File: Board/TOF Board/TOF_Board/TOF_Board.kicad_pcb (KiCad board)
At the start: 2 copper layers, 9 parts, among them J1 140-506-415-000, U1 VL53L1CBV0FY-1, U2 AT30TS74-XM8M-T

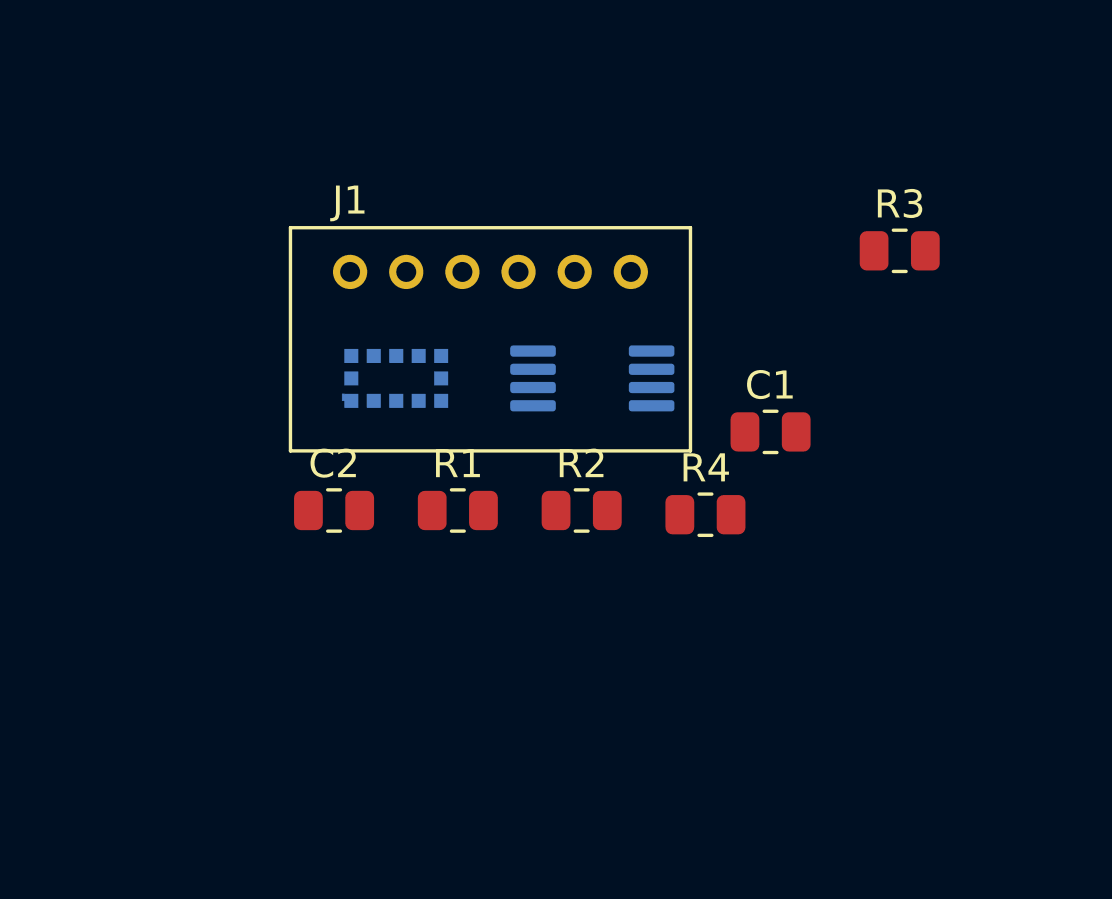
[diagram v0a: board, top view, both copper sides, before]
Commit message: added top load connector
Signed-off-by: EricTheGreat <joesmith01110000011101010111@gmail.com>
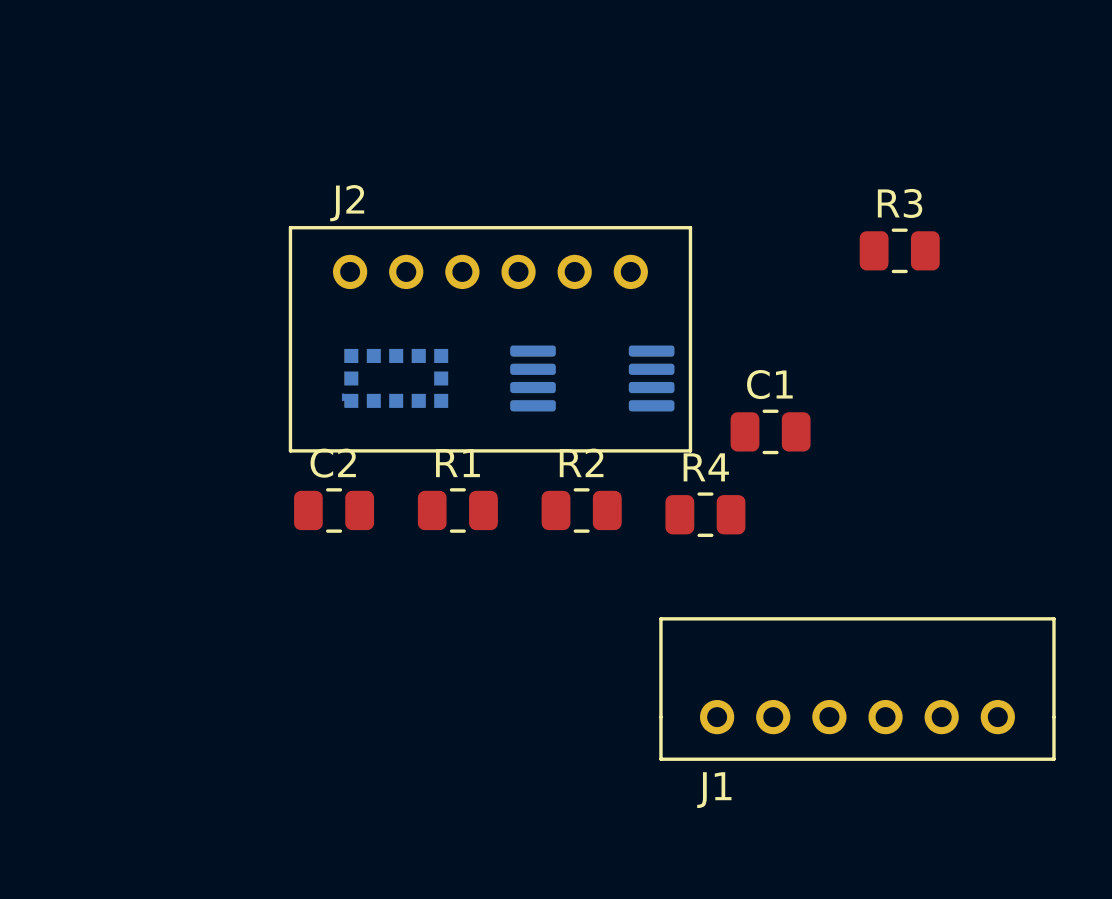
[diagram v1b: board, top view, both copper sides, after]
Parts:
- added J1: 140-506-415-001, KiCad_Cust:140-506-415-001, F.Cu at (89.5, 67.9)
- renumbered J1 to J2
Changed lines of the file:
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@@
   (net 20 "unconnected-(U2-Pad7)")
   (net 21 "unconnected-(U2-Pad8)")
+  (net 22 "unconnected-(J2-Pad1)")
+  (net 23 "unconnected-(J2-Pad2)")
+  (net 24 "unconnected-(J2-Pad3)")
+  (net 25 "unconnected-(J2-Pad4)")
+  (net 26 "unconnected-(J2-Pad5)")
+  (net 27 "unconnected-(J2-Pad6)")
   (footprint "Resistor_SMD:R_0805_2012Metric" (layer "F.Cu")
     (at 89.12 60.735)
@@
     (property "Sheetname" "")
     (attr through_hole)
-    (fp_text reference "J1" (at 0 -2.54) (layer "F.SilkS")
+    (fp_text reference "J2" (at 0 -2.54) (layer "F.SilkS")
       (effects (font (size 1 1) (thickness 0.15)))
     )
@@
     (fp_line (start -1.9977 6.2484) (end 11.9977 6.2484) (layer "F.Fab") (width 0.1))
     (pad "1" thru_hole circle (at 0 0) (size 1.2192 1.2192) (drill 0.7112) (layers *.Cu *.Mask)
+      (net 22 "unconnected-(J2-Pad1)") (pinfunction "1") (pintype "unspecified"))
+    (pad "2" thru_hole circle (at 2.000001 0) (size 1.2192 1.2192) (drill 0.7112) (layers *.Cu *.Mask)
+      (net 23 "unconnected-(J2-Pad2)") (pinfunction "2") (pintype "unspecified"))
+    (pad "3" thru_hole circle (at 4 0) (size 1.2192 1.2192) (drill 0.7112) (layers *.Cu *.Mask)
+      (net 24 "unconnected-(J2-Pad3)") (pinfunction "3") (pintype "unspecified"))
+    (pad "4" thru_hole circle (at 6.000001 0) (size 1.2192 1.2192) (drill 0.7112) (layers *.Cu *.Mask)
+      (net 25 "unconnected-(J2-Pad4)") (pinfunction "4") (pintype "unspecified"))
+    (pad "5" thru_hole circle (at 7.999999 0) (size 1.2192 1.2192) (drill 0.7112) (layers *.Cu *.Mask)
+      (net 26 "unconnected-(J2-Pad5)") (pinfunction "5") (pintype "unspecified"))
+    (pad "6" thru_hole circle (at 10 0) (size 1.2192 1.2192) (drill 0.7112) (layers *.Cu *.Mask)
+      (net 27 "unconnected-(J2-Pad6)") (pinfunction "6") (pintype "unspecified"))
+  )
+  (footprint "Resistor_SMD:R_0805_2012Metric" (layer "F.Cu")
+    (at 80.3 60.585)
+    (descr "Resistor SMD 0805 (2012 Metric), square (rectangular) end terminal, IPC_7351 nominal, (Body size source: IPC-SM-782 page 72, https://www.pcb-3d.com/wordpress/wp-content/uploads/ipc-sm-782a_amendment_1_and_2.pdf), generated with kicad-footprint-generator")
+    (tags "resistor")
+    (property "Sheetfile" "TOF_Board.kicad_sch")
+    (property "Sheetname" "")
+    (attr smd)
+    (fp_text reference "R1" (at 0 -1.65) (layer "F.SilkS")
+      (effects (font (size 1 1) (thickness 0.15)))
+    )
+    (fp_text value "2k" (at 0 1.65) (layer "F.Fab")
+      (effects (font (size 1 1) (thickness 0.15)))
+    )
+    (fp_text user "${REFERENCE}" (at 0 0) (layer "F.Fab")
+      (effects (font (size 0.5 0.5) (thickness 0.08)))
+    )
+    (fp_line (start -0.227064 0.735) (end 0.227064 0.735) (layer "F.SilkS") (width 0.12))
+    (fp_line (start -0.227064 -0.735) (end 0.227064 -0.735) (layer "F.SilkS") (width 0.12))
+    (fp_line (start -1.68 0.95) (end -1.68 -0.95) (layer "F.CrtYd") (width 0.05))
+    (fp_line (start -1.68 -0.95) (end 1.68 -0.95) (layer "F.CrtYd") (width 0.05))
+    (fp_line (start 1.68 0.95) (end -1.68 0.95) (layer "F.CrtYd") (width 0.05))
+    (fp_line (start 1.68 -0.95) (end 1.68 0.95) (layer "F.CrtYd") (width 0.05))
+    (fp_line (start 1 -0.625) (end 1 0.625) (layer "F.Fab") (width 0.1))
+    (fp_line (start -1 -0.625) (end 1 -0.625) (layer "F.Fab") (width 0.1))
+    (fp_line (start -1 0.625) (end -1 -0.625) (layer "F.Fab") (width 0.1))
+    (fp_line (start 1 0.625) (end -1 0.625) (layer "F.Fab") (width 0.1))
+    (pad "1" smd roundrect (at -0.9125 0) (size 1.025 1.4) (layers "F.Cu" "F.Paste" "F.Mask") (roundrect_rratio 0.243902)
+      (net 1 "+3V3") (pintype "passive"))
+    (pad "2" smd roundrect (at 0.9125 0) (size 1.025 1.4) (layers "F.Cu" "F.Paste" "F.Mask") (roundrect_rratio 0.243902)
+      (net 9 "Net-(R1-Pad2)") (pintype "passive"))
+    (model "${KICAD6_3DMODEL_DIR}/Resistor_SMD.3dshapes/R_0805_2012Metric.wrl"
+      (offset (xyz 0 0 0))
+      (scale (xyz 1 1 1))
+      (rotate (xyz 0 0 0))
+    )
+  )
+  (footprint "KiCad_Cust:140-506-415-001" (layer "F.Cu")
+    (at 89.535 67.945)
+    (property "Crimp Connectors" "140-941-290")
+    (property "Mates with" "140-506-210-011")
+    (property "Sheetfile" "TOF_Board.kicad_sch")
+    (property "Sheetname" "")
+    (attr through_hole)
+    (fp_text reference "J1" (at 0 2.5) (layer "F.SilkS")
+      (effects (font (size 1 1) (thickness 0.15)))
+    )
+    (fp_text value "140-506-415-001" (at 15.24 -3.81) (layer "F.SilkS") hide
+      (effects (font (size 1 1) (thickness 0.15)))
+    )
+    (fp_text user "*" (at 0 0) (layer "F.Fab")
+      (effects (font (size 1 1) (thickness 0.15)))
+    )
+    (fp_line (start 12 0) (end 12 1.5) (layer "F.SilkS") (width 0.12))
+    (fp_line (start 12 1.5) (end -2 1.5) (layer "F.SilkS") (width 0.12))
+    (fp_line (start -2 -3.5) (end 12 -3.5) (layer "F.SilkS") (width 0.12))
+    (fp_line (start -2 1.5) (end -2 0) (layer "F.SilkS") (width 0.12))
+    (fp_line (start -2 0) (end -2 -3.5) (layer "F.SilkS") (width 0.12))
+    (fp_line (start 12 -3.5) (end 12 0) (layer "F.SilkS") (width 0.12))
+    (pad "1" thru_hole circle (at 0 0) (size 1.2192 1.2192) (drill 0.7112) (layers *.Cu *.Mask)
       (net 3 "unconnected-(J1-Pad1)") (pinfunction "1") (pintype "unspecified"))
     (pad "2" thru_hole circle (at 2.000001 0) (size 1.2192 1.2192) (drill 0.7112) (layers *.Cu *.Mask)
@@
       (net 8 "unconnected-(J1-Pad6)") (pinfunction "6") (pintype "unspecified"))
   )
-  (footprint "Resistor_SMD:R_0805_2012Metric" (layer "F.Cu")
-    (at 80.3 60.585)
-    (descr "Resistor SMD 0805 (2012 Metric), square (rectangular) end terminal, IPC_7351 nominal, (Body size source: IPC-SM-782 page 72, https://www.pcb-3d.com/wordpress/wp-content/uploads/ipc-sm-782a_amendment_1_and_2.pdf), generated with kicad-footprint-generator")
-    (tags "resistor")
-    (property "Sheetfile" "TOF_Board.kicad_sch")
-    (property "Sheetname" "")
-    (attr smd)
-    (fp_text reference "R1" (at 0 -1.65) (layer "F.SilkS")
-      (effects (font (size 1 1) (thickness 0.15)))
-    )
-    (fp_text value "2k" (at 0 1.65) (layer "F.Fab")
-      (effects (font (size 1 1) (thickness 0.15)))
-    )
-    (fp_text user "${REFERENCE}" (at 0 0) (layer "F.Fab")
-      (effects (font (size 0.5 0.5) (thickness 0.08)))
-    )
-    (fp_line (start -0.227064 0.735) (end 0.227064 0.735) (layer "F.SilkS") (width 0.12))
-    (fp_line (start -0.227064 -0.735) (end 0.227064 -0.735) (layer "F.SilkS") (width 0.12))
-    (fp_line (start -1.68 0.95) (end -1.68 -0.95) (layer "F.CrtYd") (width 0.05))
-    (fp_line (start -1.68 -0.95) (end 1.68 -0.95) (layer "F.CrtYd") (width 0.05))
-    (fp_line (start 1.68 0.95) (end -1.68 0.95) (layer "F.CrtYd") (width 0.05))
-    (fp_line (start 1.68 -0.95) (end 1.68 0.95) (layer "F.CrtYd") (width 0.05))
-    (fp_line (start 1 -0.625) (end 1 0.625) (layer "F.Fab") (width 0.1))
-    (fp_line (start -1 -0.625) (end 1 -0.625) (layer "F.Fab") (width 0.1))
-    (fp_line (start -1 0.625) (end -1 -0.625) (layer "F.Fab") (width 0.1))
-    (fp_line (start 1 0.625) (end -1 0.625) (layer "F.Fab") (width 0.1))
-    (pad "1" smd roundrect (at -0.9125 0) (size 1.025 1.4) (layers "F.Cu" "F.Paste" "F.Mask") (roundrect_rratio 0.243902)
-      (net 1 "+3V3") (pintype "passive"))
-    (pad "2" smd roundrect (at 0.9125 0) (size 1.025 1.4) (layers "F.Cu" "F.Paste" "F.Mask") (roundrect_rratio 0.243902)
-      (net 9 "Net-(R1-Pad2)") (pintype "passive"))
-    (model "${KICAD6_3DMODEL_DIR}/Resistor_SMD.3dshapes/R_0805_2012Metric.wrl"
-      (offset (xyz 0 0 0))
-      (scale (xyz 1 1 1))
-      (rotate (xyz 0 0 0))
-    )
-  )
   (footprint "KiCad_Cust:XDCR_VL53L1CBV0FY-1" (layer "B.Cu")

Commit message: TOF board done (for now)
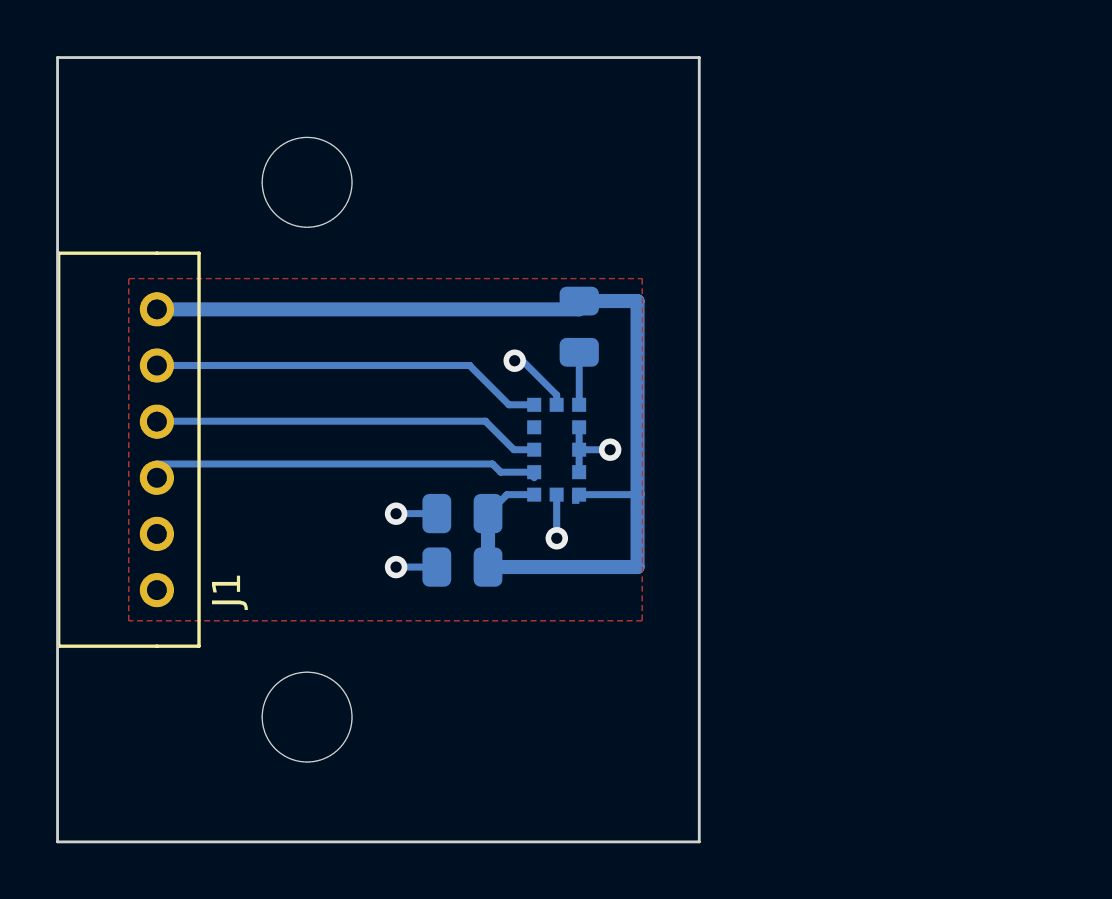
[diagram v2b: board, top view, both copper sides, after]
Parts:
- removed J2: 140-506-415-000, KiCad_Cust:140-506-415-000
- removed R1, R2, R3: 2k, Resistor_SMD:R_0805_2012Metric
- removed U2: AT30TS74-XM8M-T, Package_SO:MSOP-8_3x3mm_P0.65mm
- added REF**: MountingHole_3.2mm_M3, MountingHole:MountingHole_3.2mm_M3, F.Cu at (74.9, 48.9)
- added REF**: MountingHole_3.2mm_M3, MountingHole:MountingHole_3.2mm_M3, F.Cu at (74.9, 67.9)
- C1, C2, R4: moved to B.Cu
- moved J1 20.5 mm to (69.6, 63.4), turned to 90 degrees
- moved C1 11.4 mm to (80.5, 60.7), turned to 180 degrees
- moved R4 8.07 mm to (84.6, 54.0), turned to -90 degrees
- moved U1 6.25 mm to (83.8, 58.4), turned to 0 degrees
- moved C2 5.00 mm to (80.5, 62.6), turned to 180 degrees
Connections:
- J1 pad 1: unconnected-(J1-Pad1) -> GND
- J1 pad 2: unconnected-(J1-Pad2) -> GND
- J1 pad 3: unconnected-(J1-Pad3) -> Net-(U1-Pad10)
- J1 pad 4: unconnected-(J1-Pad4) -> Net-(U1-Pad9)
- J1 pad 5: unconnected-(J1-Pad5) -> Net-(J1-Pad5)
- J1 pad 6: unconnected-(J1-Pad6) -> +3V3
- R4 pad 1: Net-(R4-Pad1) -> +3V3
- R4 pad 2: GND -> Net-(U1-Pad5)
- U1 pad 10: Net-(R2-Pad2) -> Net-(U1-Pad10)
- U1 pad 5: Net-(R4-Pad1) -> Net-(U1-Pad5)
- U1 pad 7: Net-(R3-Pad2) -> Net-(J1-Pad5)
- U1 pad 9: Net-(R1-Pad2) -> Net-(U1-Pad9)
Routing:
- net +3V3: track 0.00 -> 38.1 mm
- net Net-(U1-Pad10): track 0.00 -> 14.3 mm
- net Net-(J1-Pad5): track 0.00 -> 14.0 mm
- net Net-(U1-Pad9): track 0.00 -> 13.9 mm
- net GND: track 0.00 -> 9.51 mm, vias 0 -> 5
- net Net-(U1-Pad5): track 0.00 -> 1.87 mm
- added copper zone on F.Cu, net GND
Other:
- board outline added: 22.9 x 27.9 mm
